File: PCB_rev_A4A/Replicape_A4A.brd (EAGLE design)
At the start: 100 x 69.6 mm, 191 parts, among them P8 F-2X23-, P9 F-2X23-, Q1 AON6758, Q2 AON6758, Q3 AON6758, Q4 NIF5002, Q5 NIF5002, Q6 NIF5002, U1 SN74AHC595PW, U10 RT8268, U11 PCA9685PW, U12 DAC088S085, U13 DRV8825PWP, U14 DRV8825PWP, U15 DRV8825PWP, U16 DRV8825PWP, U17 DRV8825PWP, U18 CAT24C256, U2 SN74AHC595PW, U3 SN74AHC595PW, U4 SN74AHC595PW, U5 SN74AHC595PW, U6 MCP16321, U7 MCP1402, U8 MCP1402, U9 MCP1402, X1 22-05-7028-02, X10 22-05-7028-02, X11 22-05-7028-02, X12 22-05-7038-03, X13 22-05-7028-02, X14 22-05-7048-04, X15 22-05-7048-04, X16 22-05-7048-04, X17 22-05-7048-04, X18 22-05-7048-04, X19 22-05-7028-02, X2 MSTBA4, X20 MSTBA4, X21 MSTBA2, X23 22-05-7028-02, X3 MSTBA2, X4 22-05-7028-02, X5 22-05-7028-02, X6 22-05-7028-02, X7 22-05-7038-03, X8 22-05-7038-03, X9 22-05-7038-03

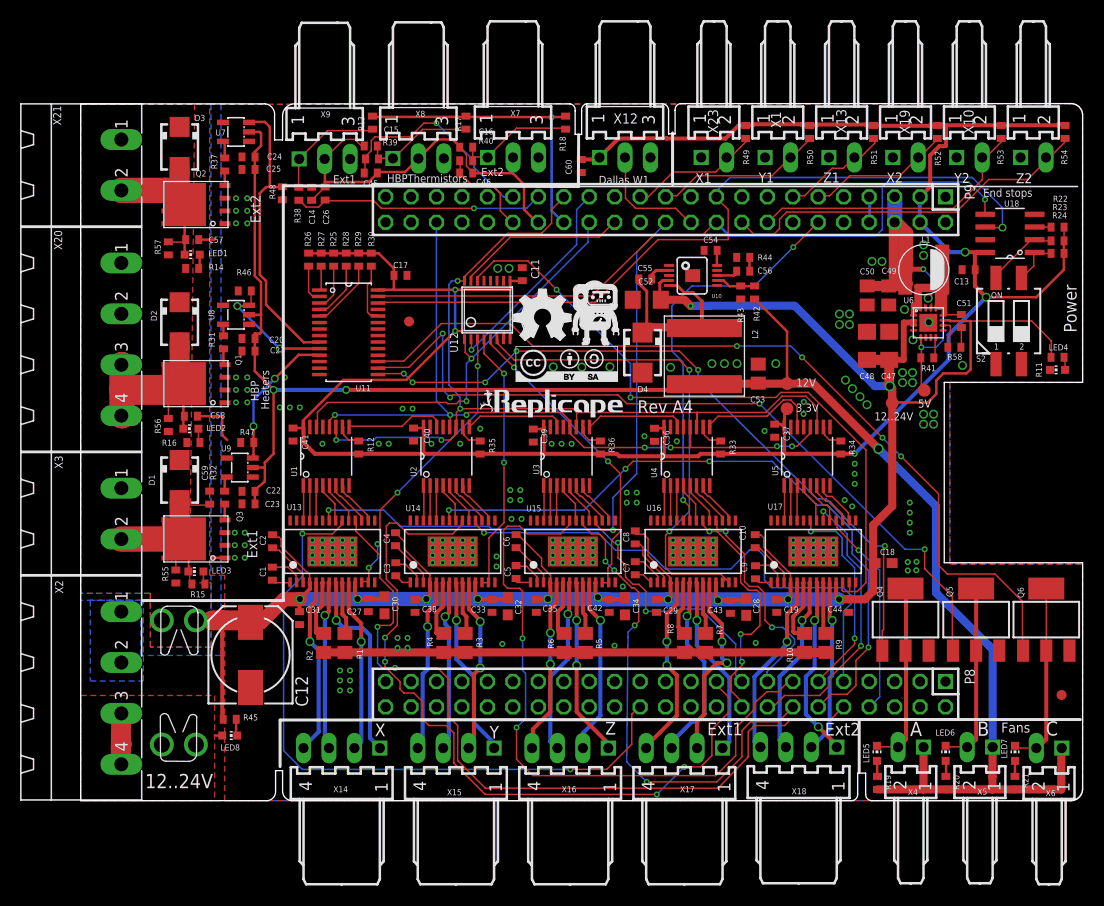
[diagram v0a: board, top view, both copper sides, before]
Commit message: Fixed the software to work with Rev A4
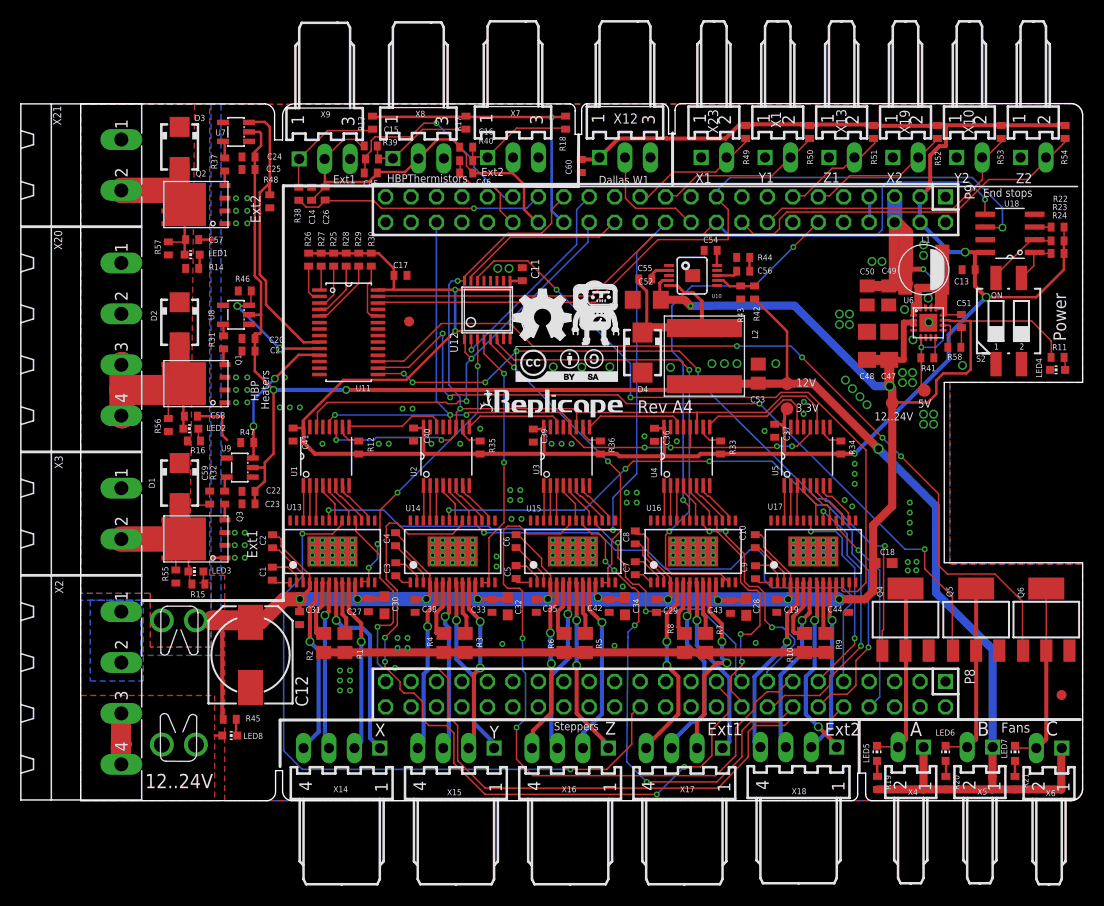
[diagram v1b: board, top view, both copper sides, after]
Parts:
- moved R48 1.48 mm to (18.9, 59.8)
- moved D1 0.30 mm to (9.88, 31.7)
- moved R16 0.16 mm to (11.3, 35.9)
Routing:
- net HEATER_EXT2: track 29.2 -> 30.0 mm

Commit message: Updated A4A
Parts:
- added EXPAND: EXPAND, con-lstb:MA05-2
- added U$3: CC-BY-SA, cc-by-sa:CC-BY-SA
- moved LOGO1 40.6 mm to (80.0, 28.6)
- moved U$1 20.3 mm to (71.2, 48.0)
- moved 3.3V 16.4 mm to (71.4, 55.5)
- moved 5V 15.1 mm to (79.8, 55.5)
- moved JP1 12.6 mm to (22.7, 55.5)
- moved R30 10.6 mm to (26.5, 43.6), turned to 180 degrees
- moved C17 8.76 mm to (29.6, 44.0), turned to 180 degrees
- moved R26 6.76 mm to (29.5, 54.5)
- moved R27 6.62 mm to (30.6, 54.5)
- moved JP2 4.70 mm to (93.2, 10.6)
- moved U12 4.40 mm to (44.9, 49.6)
- moved C11 4.39 mm to (48.4, 52.0), turned to 270 degrees
- moved R25 3.18 mm to (28.4, 54.5)
- moved U11 2.02 mm to (26.1, 48.6), turned to 270 degrees
- moved R29 1.61 mm to (26.2, 54.5)
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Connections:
- net STEP1_X renamed A1_X
- net STEP2_X renamed A2_X
- removed net STEP3_X: U13.10, X14.2
- removed net STEP3_Z: U15.10, X16.2
- removed net STEP4_X: U13.8, X14.1
- removed net STEP4_Y: U14.8, X15.1
- removed net STEP4_Z: U15.8, X16.1
- new net B1_X: U13.10, X14.1
- new net FAN4: EXPAND.9, U11.21
- new net FAN5: EXPAND.8, U11.22
- new net FAN6: EXPAND.7, U11.13
- new net HEATER_EXT3: EXPAND.5, U11.18
- new net HEATER_EXT4: EXPAND.3, U11.19
- new net HEATER_EXT5: EXPAND.1, U11.20
- new net N$2: U13.8, X14.2
- new net N$3: U14.8, X15.2
- new net N$4: U15.10, X16.1
- new net N$5: U15.8, X16.2
- new net SER6: EXPAND.10, U5.9
- new net VREF_EXT3: EXPAND.2, U12.13
- new net VREF_EXT4: EXPAND.4, U12.12
- new net VREF_EXT5: EXPAND.6, U12.11
- net STEP3_EXT1: now also X17.1; no longer X17.2
- net STEP3_EXT2: now also X18.1; no longer X18.2
- net STEP3_Y: now also X15.1; no longer X15.2
- net STEP4_EXT1: now also X17.2; no longer X17.1
- net STEP4_EXT2: now also X18.2; no longer X18.1
- net SYS_5V: no longer P9.7
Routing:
- net GND: track 61.5 -> 8.14 mm, vias 212 -> 278
- net SER6: track 0.00 -> 43.1 mm, vias 0 -> 3
- net DIR_Y: track 75.7 -> 45.7 mm, vias 4 -> 3
- net STEP_Z: track 66.8 -> 45.6 mm, vias 2 -> 3
- net STEP4_X: track 19.5 -> 0.00 mm, vias 1 -> 0
- net FAN6: track 0.00 -> 19.1 mm, vias 0 -> 1
- net FAN_1: track 71.5 -> 90.1 mm, vias 6 -> 2
- net STEP4_Y: track 18.1 -> 0.00 mm, vias 1 -> 0
- net N$3: track 0.00 -> 18.0 mm
- net STEP4_Z: track 17.9 -> 0.00 mm, vias 2 -> 0
- net STEP3_Z: track 17.9 -> 0.00 mm, vias 1 -> 0
- net B1_X: track 0.00 -> 17.8 mm
- net STEP3_X: track 17.5 -> 0.00 mm, vias 1 -> 0
- net N$4: track 0.00 -> 17.3 mm
- net N$2: track 0.00 -> 17.3 mm
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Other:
- board text added: "Rev A4A"
- board text removed: "Rev A4"
